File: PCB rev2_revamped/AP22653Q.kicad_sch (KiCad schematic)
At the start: 5 parts, among them U4 AP22815AWT-7

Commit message: asdf
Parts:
- removed C16: 10uF, Capacitor_SMD:C_0805_2012Metric, symbol Device:C
- added C25: 470uF, EasyEDA_Lib:CAP-TH_BD8.0-P3.50-D0.6-FD, symbol EasyEDA_Lib:470uF 25V Green high frequency
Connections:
- net GND: now also C25.2
- net V_IN: now also C25.1
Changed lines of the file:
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@@
 	(wire
 		(pts
-			(xy 186.69 109.22) (xy 186.69 114.3)
+			(xy 186.69 107.95) (xy 186.69 114.3)
 		)
 		(stroke
@@
 	(wire
 		(pts
-			(xy 186.69 92.71) (xy 186.69 101.6)
+			(xy 186.69 92.71) (xy 186.69 100.33)
 		)
 		(stroke
@@
 	)
 	(symbol
+		(lib_id "EasyEDA_Lib:470uF 25V Green high frequency")
+		(at 186.69 104.14 270)
+		(unit 1)
+		(exclude_from_sim no)
+		(in_bom yes)
+		(on_board yes)
+		(dnp no)
+		(fields_autoplaced yes)
+		(property "Reference" "C25"
+			(at 190.5 103.5049 90)
+			(effects
+				(font
+					(size 1.27 1.27)
+				)
+				(justify left)
+			)
+		)
+		(property "Value" "470uF"
+			(at 186.69 104.14 0)
+			(effects
+				(font
+					(size 1.27 1.27)
+				)
+			)
+		)
+		(property "Footprint" "EasyEDA_Lib:CAP-TH_BD8.0-P3.50-D0.6-FD"
+			(at 186.69 104.14 0)
+			(effects
+				(font
+					(size 1.27 1.27)
+				)
+				(hide yes)
+			)
+		)
+		(property "Datasheet" "https://item.szlcsc.com/datasheet/GR477M025F14RR0VL4FP0/5573.html"
+			(at 186.69 104.14 0)
+			(effects
+				(font
+					(size 1.27 1.27)
+				)
+				(hide yes)
+			)
+		)
+		(property "Description" "Capacitance:470uF Tolerance:±20% Tolerance:±20% Voltage Rating:25V Pin Spacing:3.5mm Diameter:8mm Height - Seated (Max):14mm Lifetime:3000hrs@105°C Operating Temperature:-40°C~+105°C Operating Temperature:-40°C~+105°C"
+			(at 186.69 104.14 0)
+			(effects
+				(font
+					(size 1.27 1.27)
+				)
+				(hide yes)
+			)
+		)
+		(property "Manufacturer Part" "GR477M025F14RR0VL4FP0"
+			(at 186.69 104.14 0)
+			(effects
+				(font
+					(size 1.27 1.27)
+				)
+				(hide yes)
+			)
+		)
+		(property "Manufacturer" "Chengx(承兴)"
+			(at 186.69 104.14 0)
+			(effects
+				(font
+					(size 1.27 1.27)
+				)
+				(hide yes)
+			)
+		)
+		(property "Supplier Part" "C5154"
+			(at 186.69 104.14 0)
+			(effects
+				(font
+					(size 1.27 1.27)
+				)
+				(hide yes)
+			)
+		)
+		(property "Supplier" "LCSC"
+			(at 186.69 104.14 0)
+			(effects
+				(font
+					(size 1.27 1.27)
+				)
+				(hide yes)
+			)
+		)
+		(property "LCSC Part Name" "绿色 470uF ±20% 25V"
+			(at 186.69 104.14 0)
+			(effects
+				(font
+					(size 1.27 1.27)
+				)
+				(hide yes)
+			)
+		)
+		(pin "2"
+		)
+		(pin "1"
+		)
+		(instances
+			(project ""
+				(path "/adf54578-0edd-4ea8-a516-35041fcd2885/905a8709-dadb-438d-a64a-98151fb9a03c"
+					(reference "C25")
+					(unit 1)
+				)
+			)
+		)
+	)
+	(symbol
 		(lib_id "Device:R_US")
 		(at 167.64 85.09 0)
@@
 					(unit 1)
 				)
-			)
-		)
-	)
-	(symbol
-		(lib_id "Device:C")
-		(at 186.69 105.41 0)
-		(unit 1)
-		(exclude_from_sim no)
-		(in_bom yes)
-		(on_board yes)
-		(dnp no)
-		(fields_autoplaced yes)
-		(property "Reference" "C16"
-			(at 190.5 104.1399 0)
-			(effects
-				(font
-					(size 1.27 1.27)
-				)
-				(justify left)
-			)
-		)
-		(property "Value" "10uF"
-			(at 190.5 106.6799 0)
-			(effects
-				(font
-					(size 1.27 1.27)
-				)
-				(justify left)
-			)
-		)
-		(property "Footprint" "Capacitor_SMD:C_0805_2012Metric"
-			(at 187.6552 109.22 0)
-			(effects
-				(font
-					(size 1.27 1.27)
-				)
-				(hide yes)
-			)
-		)
-		(property "Datasheet" "https://www.digikey.com/en/products/detail/murata-electronics/GCM21BR71A106KE22K/4903979"
-			(at 186.69 105.41 0)
-			(effects
-				(font
-					(size 1.27 1.27)
-				)
-				(hide yes)
-			)
-		)
-		(property "Description" "Unpolarized capacitor"
-			(at 186.69 105.41 0)
-			(effects
-				(font
-					(size 1.27 1.27)
-				)
-				(hide yes)
-			)
-		)
-		(property "AVAILABILITY" ""
-			(at 186.69 105.41 0)
-			(effects
-				(font
-					(size 1.27 1.27)
-				)
-				(hide yes)
-			)
-		)
-		(property "Color " ""
-			(at 186.69 105.41 0)
-			(effects
-				(font
-					(size 1.27 1.27)
-				)
-				(hide yes)
-			)
-		)
-		(property "DESCRIPTION" ""
-			(at 186.69 105.41 0)
-			(effects
-				(font
-					(size 1.27 1.27)
-				)
-				(hide yes)
-			)
-		)
-		(property "PACKAGE" ""
-			(at 186.69 105.41 0)
-			(effects
-				(font
-					(size 1.27 1.27)
-				)
-				(hide yes)
-			)
-		)
-		(property "PRICE" ""
-			(at 186.69 105.41 0)
-			(effects
-				(font
-					(size 1.27 1.27)
-				)
-				(hide yes)
-			)
-		)
-		(property "Part #" "GCM21BR71A106KE22K"
-			(at 186.69 105.41 0)
-			(effects
-				(font
-					(size 1.27 1.27)
-				)
-				(hide yes)
-			)
-		)
-		(pin "1"
-		)
-		(pin "2"
-		)
-		(instances
-			(project "PCB Rev2"
-				(path "/adf54578-0edd-4ea8-a516-35041fcd2885/905a8709-dadb-438d-a64a-98151fb9a03c"
-					(reference "C16")
-					(unit 1)
-				)

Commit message: a
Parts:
- removed R12: 10k, symbol Device:R_US
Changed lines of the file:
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@@
-	(wire
-		(pts
-			(xy 167.64 97.79) (xy 167.64 88.9)
-		)
-		(stroke
-			(width 0)
-			(type default)
-		)
-	)
 	(wire
 		(pts
@@
 	(wire
 		(pts
-			(xy 167.64 81.28) (xy 167.64 78.74)
-		)
-		(stroke
-			(width 0)
-			(type default)
-		)
-	)
-	(wire
-		(pts
-			(xy 167.64 78.74) (xy 186.69 78.74)
-		)
-		(stroke
-			(width 0)
-			(type default)
-		)
-	)
-	(wire
-		(pts
 			(xy 146.05 114.3) (xy 146.05 118.11)
 		)
@@
 	(wire
 		(pts
-			(xy 186.69 78.74) (xy 186.69 92.71)
-		)
-		(stroke
-			(width 0)
-			(type default)
-		)
-	)
-	(wire
-		(pts
 			(xy 120.65 95.25) (xy 120.65 114.3)
 		)
@@
 		(pts
 			(xy 171.45 109.22) (xy 171.45 114.3)
-		)
-		(stroke
-			(width 0)
-			(type default)
-		)
-	)
-	(wire
-		(pts
-			(xy 165.1 97.79) (xy 167.64 97.79)
 		)
 		(stroke
@@
 					(unit 1)
 				)
-			)
-		)
-	)
-	(symbol
-		(lib_id "Device:R_US")
-		(at 167.64 85.09 0)
-		(unit 1)
-		(exclude_from_sim no)
-		(in_bom yes)
-		(on_board yes)
-		(dnp no)
-		(fields_autoplaced yes)
-		(property "Reference" "R12"
-			(at 170.18 83.8199 0)
-			(effects
-				(font
-					(size 1.27 1.27)
-				)
-				(justify left)
-			)
-		)
-		(property "Value" "10k"
-			(at 170.18 86.3599 0)
-			(effects
-				(font
-					(size 1.27 1.27)
-				)
-				(justify left)
-			)
-		)
-		(property "Footprint" ""
-			(at 168.656 85.344 90)
-			(effects
-				(font
-					(size 1.27 1.27)
-				)
-				(hide yes)
-			)
-		)
-		(property "Datasheet" "~"
-			(at 167.64 85.09 0)
-			(effects
-				(font
-					(size 1.27 1.27)
-				)
-				(hide yes)
-			)
-		)
-		(property "Description" "Resistor, US symbol"
-			(at 167.64 85.09 0)
-			(effects
-				(font
-					(size 1.27 1.27)
-				)
-				(hide yes)
-			)
-		)
-		(pin "2"
-		)
-		(pin "1"
-		)
-		(instances
-			(project ""
-				(path "/adf54578-0edd-4ea8-a516-35041fcd2885/905a8709-dadb-438d-a64a-98151fb9a03c"
-					(reference "R12")
-					(unit 1)
-				)

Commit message: added i2c
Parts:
- removed C18: 0.1uF, Capacitor_SMD:C_0603_1608Metric, symbol Device:C
- added C1: 100uF, EasyEDA_Lib:CAP-TH_BD8.0-P3.50-D0.6-FD, symbol EasyEDA_Lib:50V 100uF 8X12
- added C2: 1uF, Capacitor_SMD:C_0805_2012Metric, symbol Device:C
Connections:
- net GND: now also C1.2, C2.2
- net V_IN: now also C2.1
- net V_OUT: now also C1.1
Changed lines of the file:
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@@
+	)
+	(junction
+		(at 101.6 92.71)
+		(diameter 0)
+		(color 0 0 0 0)
 	)
 	(junction
@@
 	)
 	(junction
+		(at 110.49 114.3)
+		(diameter 0)
+		(color 0 0 0 0)
+	)
+	(junction
 		(at 171.45 92.71)
 		(diameter 0)
@@
 	(wire
 		(pts
+			(xy 101.6 114.3) (xy 101.6 109.22)
+		)
+		(stroke
+			(width 0)
+			(type default)
+		)
+	)
+	(wire
+		(pts
 			(xy 110.49 114.3) (xy 120.65 114.3)
 		)
@@
 	(wire
 		(pts
+			(xy 101.6 92.71) (xy 110.49 92.71)
+		)
+		(stroke
+			(width 0)
+			(type default)
+		)
+	)
+	(wire
+		(pts
 			(xy 146.05 114.3) (xy 146.05 118.11)
 		)
@@
 	(wire
 		(pts
-			(xy 97.79 92.71) (xy 110.49 92.71)
+			(xy 97.79 92.71) (xy 101.6 92.71)
+		)
+		(stroke
+			(width 0)
+			(type default)
+		)
+	)
+	(wire
+		(pts
+			(xy 110.49 114.3) (xy 101.6 114.3)
 		)
 		(stroke
@@
 		(pts
 			(xy 171.45 109.22) (xy 171.45 114.3)
+		)
+		(stroke
+			(width 0)
+			(type default)
+		)
+	)
+	(wire
+		(pts
+			(xy 101.6 92.71) (xy 101.6 101.6)
 		)
 		(stroke
@@
 	(symbol
 		(lib_id "Device:C")
-		(at 171.45 105.41 0)
-		(unit 1)
-		(exclude_from_sim no)
-		(in_bom yes)
-		(on_board yes)
-		(dnp no)
-		(fields_autoplaced yes)
-		(property "Reference" "C18"
-			(at 175.26 104.1399 0)
-			(effects
-				(font
-					(size 1.27 1.27)
-				)
-				(justify left)
-			)
-		)
-		(property "Value" "0.1uF"
-			(at 175.26 106.6799 0)
-			(effects
-				(font
-					(size 1.27 1.27)
-				)
-				(justify left)
-			)
-		)
-		(property "Footprint" "Capacitor_SMD:C_0603_1608Metric"
-			(at 172.4152 109.22 0)
-			(effects
-				(font
-					(size 1.27 1.27)
-				)
-				(hide yes)
-			)
-		)
-		(property "Datasheet" "https://www.digikey.com/en/products/detail/kemet/C0603C104K8RACAUTO/8572409"
-			(at 171.45 105.41 0)
-			(effects
-				(font
-					(size 1.27 1.27)
-				)
-				(hide yes)
-			)
-		)
-		(property "Description" "Unpolarized capacitor"
-			(at 171.45 105.41 0)
-			(effects
-				(font
-					(size 1.27 1.27)
-				)
-				(hide yes)
-			)
-		)
-		(property "AVAILABILITY" ""
-			(at 171.45 105.41 0)
-			(effects
-				(font
-					(size 1.27 1.27)
-				)
-				(hide yes)
-			)
-		)
-		(property "Color " ""
-			(at 171.45 105.41 0)
-			(effects
-				(font
-					(size 1.27 1.27)
-				)
-				(hide yes)
-			)
-		)
-		(property "DESCRIPTION" ""
-			(at 171.45 105.41 0)
-			(effects
-				(font
-					(size 1.27 1.27)
-				)
-				(hide yes)
-			)
-		)
-		(property "PACKAGE" ""
-			(at 171.45 105.41 0)
-			(effects
-				(font
-					(size 1.27 1.27)
-				)
-				(hide yes)
-			)
-		)
-		(property "PRICE" ""
-			(at 171.45 105.41 0)
-			(effects
-				(font
-					(size 1.27 1.27)
-				)
-				(hide yes)
-			)
-		)
-		(property "Part #" "C0603C104K8RACAUTO"
-			(at 171.45 105.41 0)
-			(effects
-				(font
-					(size 1.27 1.27)
-				)
-				(hide yes)
-			)
-		)
-		(pin "2"
-		)
-		(pin "1"
-		)
-		(instances
-			(project "Data Logger Rev1"
-				(path "/adf54578-0edd-4ea8-a516-35041fcd2885/905a8709-dadb-438d-a64a-98151fb9a03c"
-					(reference "C18")
-					(unit 1)
-				)
-			)
-		)
-	)
-	(symbol
-		(lib_id "Device:C")
 		(at 110.49 105.41 0)
 		(unit 1)
@@
 					(unit 1)
 				)
+			)
+		)
+	)
+	(symbol
+		(lib_id "Device:C")
+		(at 171.45 105.41 0)
+		(unit 1)
+		(exclude_from_sim no)
+		(in_bom yes)
+		(on_board yes)
+		(dnp no)
+		(fields_autoplaced yes)
+		(property "Reference" "C2"
+			(at 175.26 104.1399 0)
+			(effects
+				(font
+					(size 1.27 1.27)
+				)
+				(justify left)
+			)
+		)
+		(property "Value" "1uF"
+			(at 175.26 106.6799 0)
+			(effects
+				(font
+					(size 1.27 1.27)
+				)
+				(justify left)
+			)
+		)
+		(property "Footprint" "Capacitor_SMD:C_0805_2012Metric"
+			(at 172.4152 109.22 0)
+			(effects
+				(font
+					(size 1.27 1.27)
+				)
+				(hide yes)
+			)
+		)
+		(property "Datasheet" "https://www.digikey.com/en/products/detail/taiyo-yuden/UMK212B7105KGHT/4811080"
+			(at 171.45 105.41 0)
+			(effects
+				(font
+					(size 1.27 1.27)
+				)
+				(hide yes)
+			)
+		)
+		(property "Description" "Unpolarized capacitor"
+			(at 171.45 105.41 0)
+			(effects
+				(font
+					(size 1.27 1.27)
+				)
+				(hide yes)
+			)
+		)
+		(property "Part #" "UMK212B7105KGHT"
+			(at 171.45 105.41 0)
+			(effects
+				(font
+					(size 1.27 1.27)
+				)
+				(hide yes)
+			)
+		)
+		(property "AVAILABILITY" ""
+			(at 171.45 105.41 0)
+			(effects
+				(font
+					(size 1.27 1.27)
+				)
+				(hide yes)
+			)
+		)
+		(property "Color " ""
+			(at 171.45 105.41 0)
+			(effects
+				(font
+					(size 1.27 1.27)
+				)
+				(hide yes)
+			)
+		)
+		(property "DESCRIPTION" ""
+			(at 171.45 105.41 0)
+			(effects
+				(font
+					(size 1.27 1.27)
+				)
+				(hide yes)
+			)
+		)
+		(property "PACKAGE" ""
+			(at 171.45 105.41 0)
+			(effects
+				(font
+					(size 1.27 1.27)
+				)
+				(hide yes)
+			)
+		)
+		(property "PRICE" ""
+			(at 171.45 105.41 0)
+			(effects
+				(font
+					(size 1.27 1.27)
+				)
+				(hide yes)
+			)
+		)
+		(pin "2"
+		)
+		(pin "1"
+		)
+		(instances
+			(project "PCB Rev2"
+				(path "/adf54578-0edd-4ea8-a516-35041fcd2885/905a8709-dadb-438d-a64a-98151fb9a03c"
+					(reference "C2")
+					(unit 1)
+				)
+			)
+		)
+	)
+	(symbol
+		(lib_id "EasyEDA_Lib:50V 100uF 8X12")
+		(at 101.6 105.41 270)
+		(unit 1)
+		(exclude_from_sim no)
+		(in_bom yes)
+		(on_board yes)
+		(dnp no)
+		(fields_autoplaced yes)
+		(property "Reference" "C1"
+			(at 105.41 104.7749 90)
+			(effects
+				(font
+					(size 1.27 1.27)
+				)
+				(justify left)
+			)
+		)
+		(property "Value" "100uF"
+			(at 101.6 105.41 0)
+			(effects
+				(font
+					(size 1.27 1.27)
+				)
+				(hide yes)
+			)
+		)
+		(property "Footprint" "EasyEDA_Lib:CAP-TH_BD8.0-P3.50-D0.6-FD"
+			(at 101.6 105.41 0)
+			(effects
+				(font
+					(size 1.27 1.27)
+				)
+				(hide yes)
+			)
+		)
+		(property "Datasheet" "https://item.szlcsc.com/datasheet/KM107M050F12RR0VH2FP0/3130.html"
+			(at 101.6 105.41 0)
+			(effects
+				(font
+					(size 1.27 1.27)
+				)
+				(hide yes)
+			)
+		)
+		(property "Description" "Capacitance:100uF Tolerance:±20% Tolerance:±20% Voltage Rating:50V Pin Spacing:3.5mm Diameter:8mm Height - Seated (Max):12mm Lifetime:2000hrs@105°C"
+			(at 101.6 105.41 0)
+			(effects
+				(font
+					(size 1.27 1.27)
+				)
+				(hide yes)
+			)
+		)
+		(property "Manufacturer Part" "KM107M050F12RR0VH2FP0"
+			(at 101.6 105.41 0)
+			(effects
+				(font
+					(size 1.27 1.27)
+				)
+				(hide yes)
+			)
+		)
+		(property "Manufacturer" "Chengx(承兴)"
+			(at 101.6 105.41 0)
+			(effects
+				(font
+					(size 1.27 1.27)
+				)
+				(hide yes)
+			)
+		)
+		(property "Supplier Part" "C2749"
+			(at 101.6 105.41 0)
+			(effects
+				(font
+					(size 1.27 1.27)
+				)
+				(hide yes)
+			)
+		)
+		(property "Supplier" "LCSC"
+			(at 101.6 105.41 0)
+			(effects
+				(font
+					(size 1.27 1.27)
+				)
+				(hide yes)
+			)
+		)
+		(property "LCSC Part Name" "100uF ±20% 50V"
+			(at 101.6 105.41 0)
+			(effects
+				(font
+					(size 1.27 1.27)
+				)
+				(hide yes)
+			)
+		)
+		(pin "1"
+		)
+		(pin "2"
+		)
+		(instances
+			(project ""
+				(path "/adf54578-0edd-4ea8-a516-35041fcd2885/905a8709-dadb-438d-a64a-98151fb9a03c"
+					(reference "C1")
+					(unit 1)
+				)

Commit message: final revision
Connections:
- no-connect marks 0 -> 1
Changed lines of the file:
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@@
 		(color 0 0 0 0)
+	)
+	(no_connect
+		(at 165.1 97.79)
 	)
 	(wire

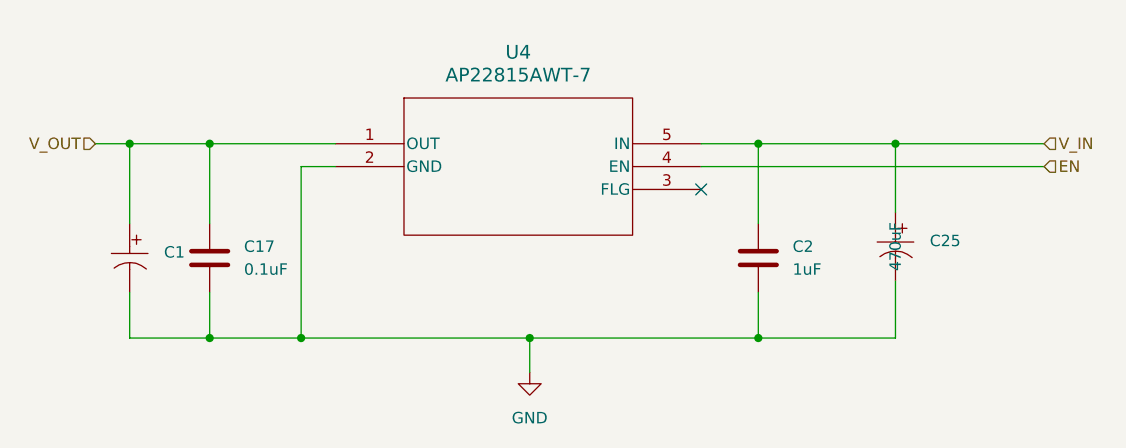
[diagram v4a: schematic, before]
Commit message: final touches
-added pull down for en
-didnt change tx rx since its software swappable
-connected lora to vcc, shifted pins since they were mapped wrong too.
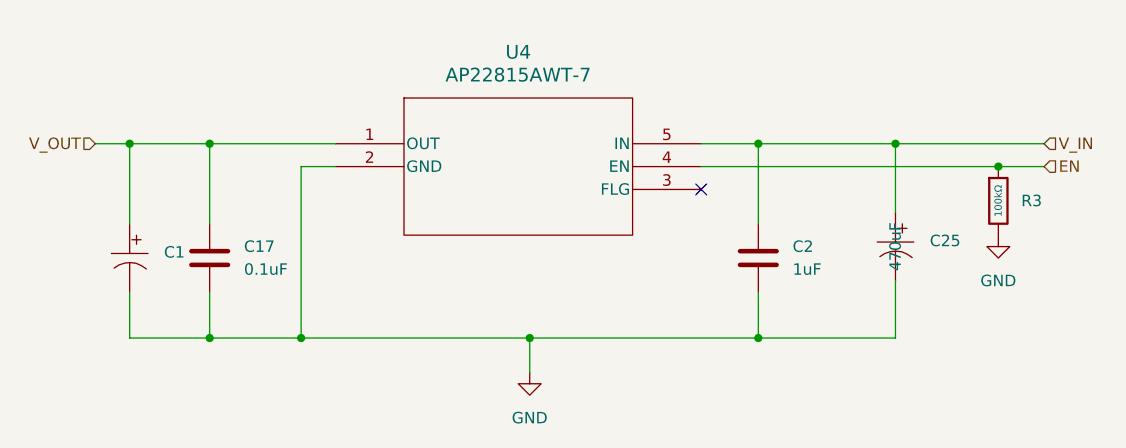
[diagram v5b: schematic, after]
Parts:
- added R3: 100kΩ, PCM_JLCPCB:R_0603, symbol PCM_JLCPCB-Resistors:0603,100kΩ
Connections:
- net EN: now also R3.1
- net GND: now also R3.2
